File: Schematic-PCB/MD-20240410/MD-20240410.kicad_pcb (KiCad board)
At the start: 2 copper layers, 100.5 x 56.4 mm, 52 parts, among them J1 Conn_01x05_Pin, J2 Conn_01x04_Pin, J3 Conn_01x02_Pin, J4 Conn_01x02_Pin, J5 Conn_01x02_Pin, J6 Conn_01x02_Pin, J7 Conn_01x02_Pin, J8 Conn_01x15_Pin, Q2 PMOS, Q3 NMOS, Q4 NMOS

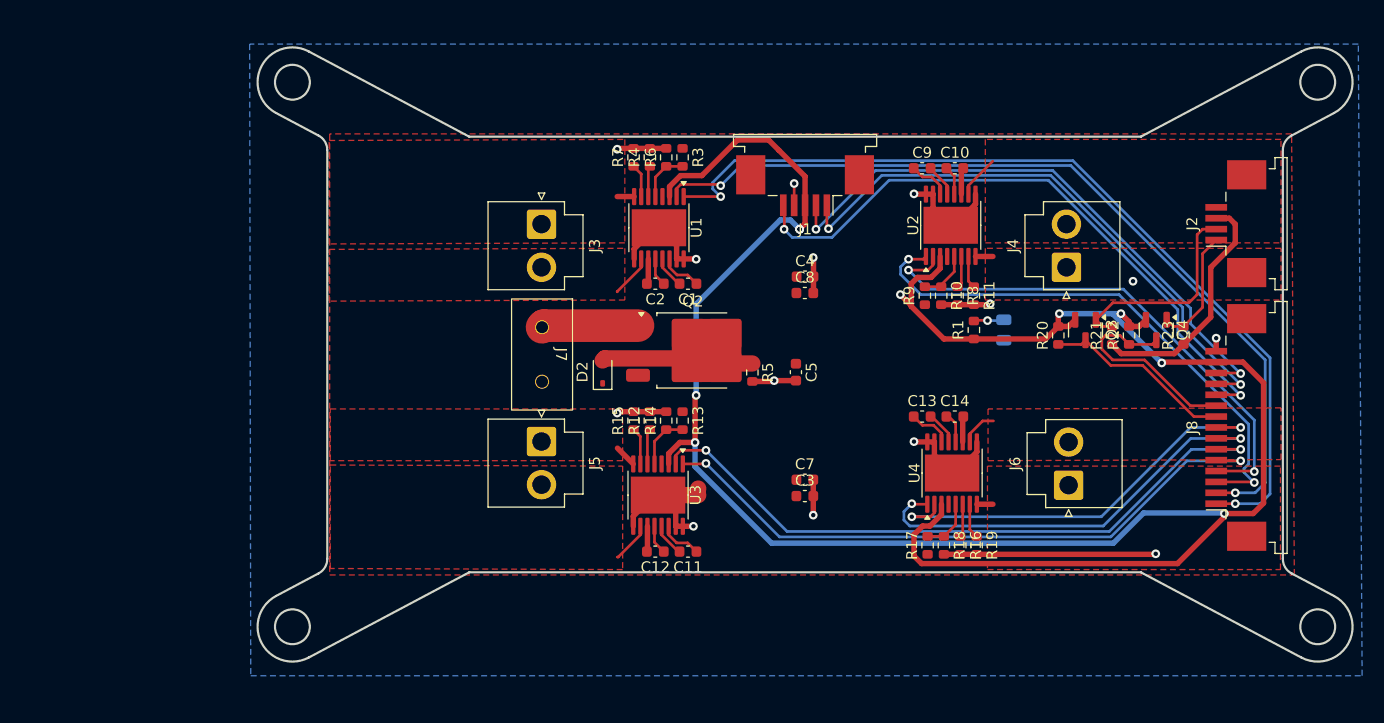
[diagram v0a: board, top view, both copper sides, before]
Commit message: MD回路のDR修正版-1
SLEEPは修正していません
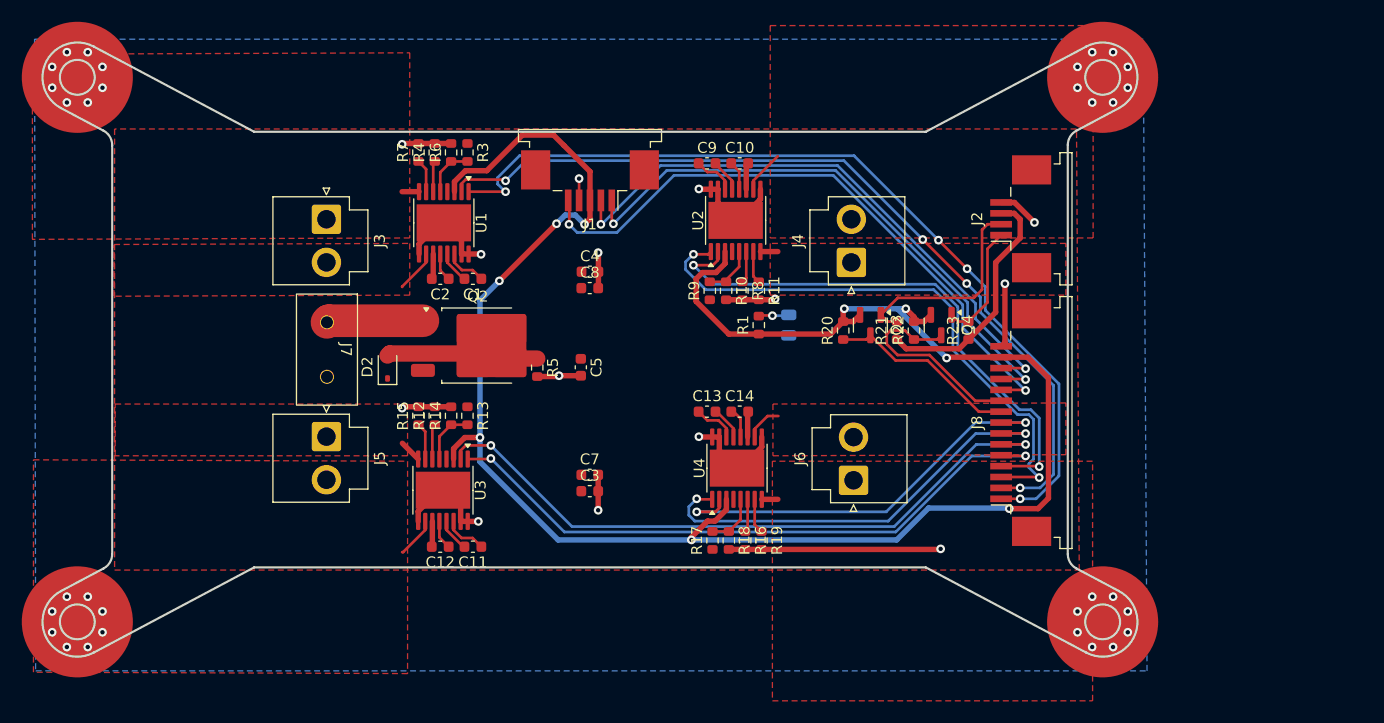
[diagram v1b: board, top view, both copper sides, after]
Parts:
- moved U1 19.8 mm to (116.8, 75.4)
- moved C1 19.8 mm to (119.5, 80.5)
- moved C10 19.8 mm to (144.0, 70.0)
- moved C11 19.8 mm to (119.5, 105.2)
- moved C12 19.8 mm to (116.5, 105.2)
- moved C13 19.8 mm to (141.0, 92.8)
- moved C14 19.8 mm to (144.0, 92.8)
- moved C2 19.8 mm to (116.5, 80.5)
- moved C3 19.8 mm to (130.2, 100.0)
- moved C4 19.8 mm to (130.2, 79.9)
- moved C5 19.8 mm to (129.4, 88.7)
- moved C7 19.8 mm to (130.2, 98.5)
- moved C8 19.8 mm to (130.2, 81.4)
- moved C9 19.8 mm to (141.0, 70.0)
- moved D1 19.8 mm to (148.5, 84.8)
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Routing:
- net +3.3V: track 209.8 -> 176.8 mm
- net GND: track 87.5 -> 92.4 mm, vias 14 -> 46
- net EN-2: track 50.5 -> 52.7 mm
- net PH-2: track 48.9 -> 51.0 mm
- net EN-1: track 82.3 -> 81.9 mm, vias 2 -> 4
- net PH-1: track 79.3 -> 78.9 mm, vias 2 -> 4

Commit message: Auto stash before merge of "main" and "origin/main"
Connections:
- J1 pad 3: +3.3V -> SLEEP-1
- J8 pad 14: +3.3V -> SLEEP-1
- Q3 pad 2: +3.3V -> SLEEP-1
- Q4 pad 2: +3.3V -> SLEEP-1
- R1 pad 1: +3.3V -> SLEEP-1
- R13 pad 1: SLEEP-3 -> SLEEP-1
- R17 pad 1: SLEEP-4 -> SLEEP-1
- R20 pad 2: +3.3V -> SLEEP-1
- R22 pad 2: +3.3V -> SLEEP-1
- R9 pad 1: SLEEP-2 -> SLEEP-1
- U1 pad 3: +3.3V -> SLEEP-1
- U2 pad 3: +3.3V -> SLEEP-1
- U3 pad 3: +3.3V -> SLEEP-1
- U4 pad 3: +3.3V -> SLEEP-1
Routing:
- net SLEEP-1: track 0.00 -> 187.9 mm, vias 0 -> 9
- net +3.3V: track 176.8 -> 0.00 mm, vias 9 -> 0

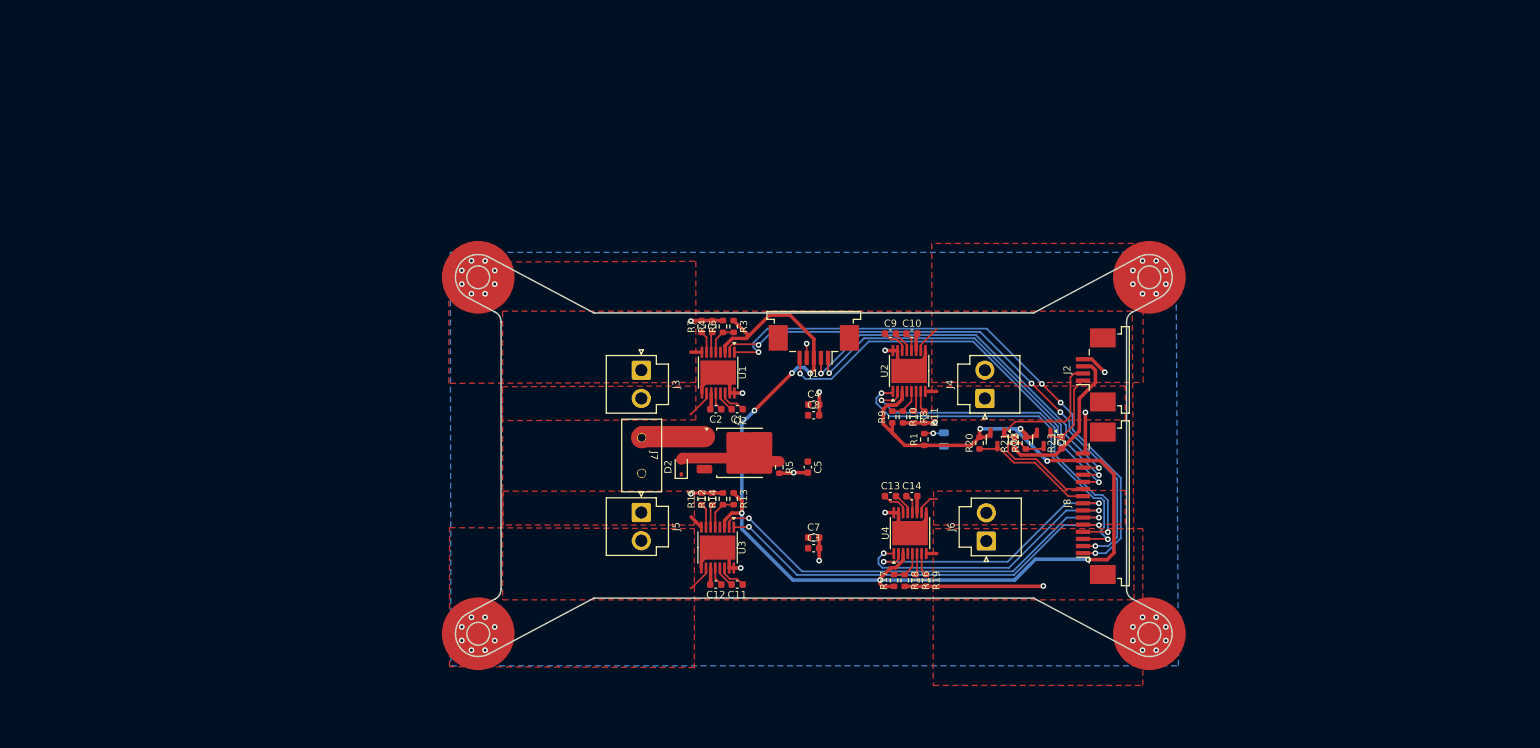
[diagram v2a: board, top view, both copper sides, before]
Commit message: MDの回路図/PCBを更新
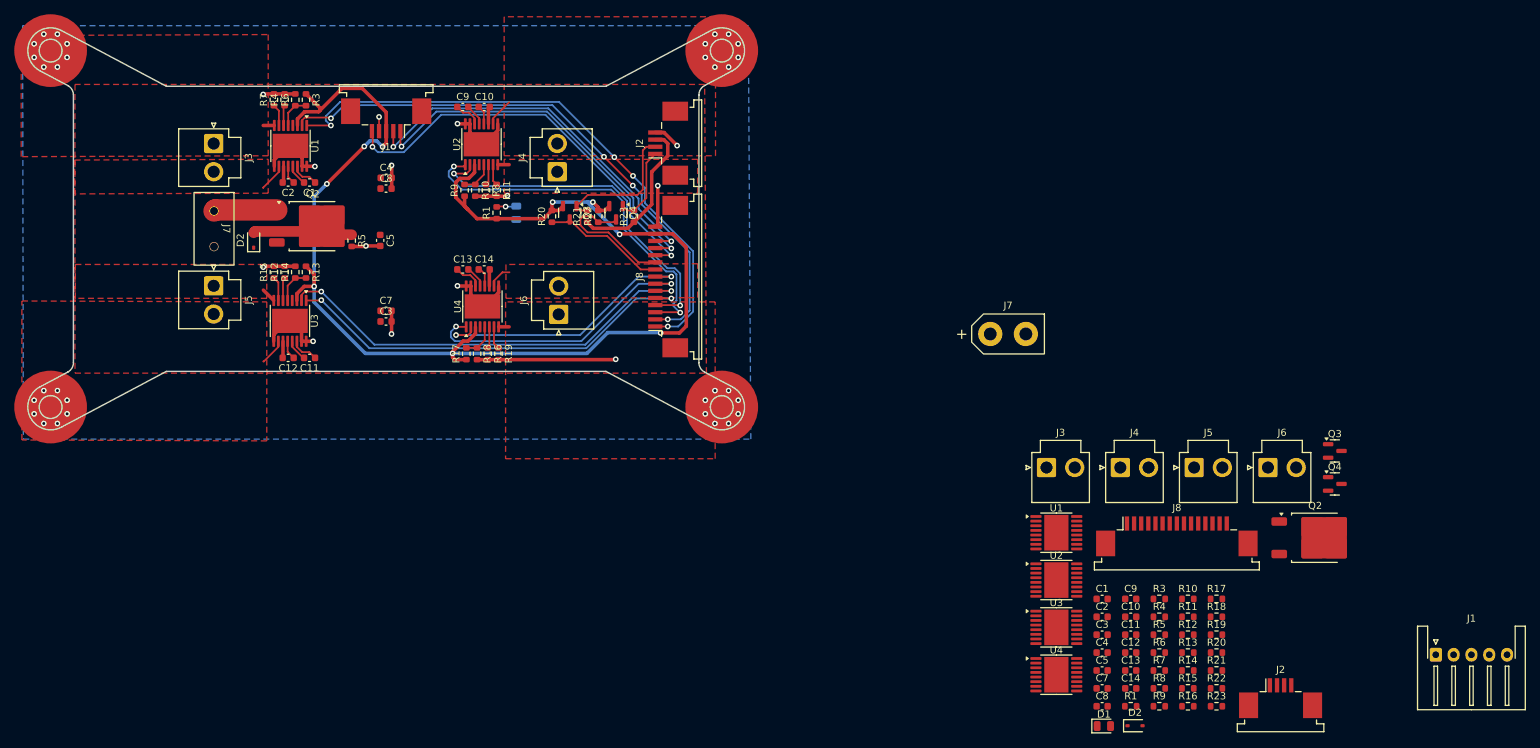
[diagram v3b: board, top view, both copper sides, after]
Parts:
- removed the C1 at (119.5, 80.5)
- removed the C10 at (144.0, 70.0)
- removed the C11 at (119.5, 105.2)
- removed the C12 at (116.5, 105.2)
- removed the C13 at (141.0, 92.8)
- removed the C14 at (144.0, 92.8)
- removed the C2 at (116.5, 80.5)
- removed the C3 at (130.2, 100.0)
- removed the C4 at (130.2, 79.9)
- removed the C5 at (129.4, 88.7)
- removed the C7 at (130.2, 98.5)
- removed the C8 at (130.2, 81.4)
- removed the C9 at (141.0, 70.0)
- removed the D1 at (148.5, 84.8)
- removed the D2 at (111.7, 88.7)
- removed the J1 at (130.2, 71.5)
- removed the J2 at (169.8, 75.0)
- removed the J3 at (106.0, 75.1)
- removed the J4 at (154.2, 79.0)
- removed the J5 at (106.0, 95.0)
- removed the J6 at (154.4, 99.0)
- removed the J7 at (106.1, 87.0)
- removed the J8 at (169.8, 93.8)
- removed the Q2 at (120.0, 86.7)
- removed the Q3 at (156.0, 84.8)
- removed the Q4 at (162.5, 84.8)
- removed the R1 at (145.8, 84.8)
- removed the R10 at (142.8, 81.7)
- removed the R11 at (145.8, 81.7)
- removed the R12 at (116.0, 93.1)
- removed the R13 at (119.0, 93.1)
- removed the R14 at (117.5, 93.1)
- removed the R15 at (114.5, 93.1)
- removed the R16 at (144.5, 104.6)
- removed the R17 at (141.5, 104.6)
- removed the R18 at (143.0, 104.6)
- removed the R19 at (146.0, 104.6)
- removed the R20 at (153.5, 85.3)
- removed the R21 at (158.4, 85.3)
- removed the R22 at (160.0, 85.3)
- removed the R23 at (165.0, 85.3)
- removed the R3 at (119.0, 69.0)
- removed the R4 at (116.0, 69.0)
- removed the R5 at (125.4, 88.7)
- removed the R6 at (117.5, 69.0)
- removed the R7 at (114.5, 69.0)
- removed the R8 at (144.2, 81.7)
- removed the R9 at (141.2, 81.7)
- removed the U1 at (116.8, 75.4)
- removed the U2 at (143.6, 75.2)
- removed the U3 at (116.8, 100.0)
- removed the U4 at (143.8, 97.9)
- added C1: 22n, Capacitor_SMD:C_0603_1608Metric, F.Cu at (59.5, 48.8)
- added C1: 22n, Capacitor_SMD:C_0603_1608Metric, F.Cu at (170.7, 107.2)
- added C10: 220n, Capacitor_SMD:C_0603_1608Metric, F.Cu at (174.7, 109.7)
- added C10: 220n, Capacitor_SMD:C_0603_1608Metric, F.Cu at (84.0, 38.1)
- added C11: 22n, Capacitor_SMD:C_0603_1608Metric, F.Cu at (174.7, 112.2)
- added C11: 22n, Capacitor_SMD:C_0603_1608Metric, F.Cu at (59.5, 73.3)
- added C12: 220n, Capacitor_SMD:C_0603_1608Metric, F.Cu at (174.7, 114.7)
- added C12: 220n, Capacitor_SMD:C_0603_1608Metric, F.Cu at (56.5, 73.3)
- added C13: 22n, Capacitor_SMD:C_0603_1608Metric, F.Cu at (174.7, 117.2)
- added C13: 22n, Capacitor_SMD:C_0603_1608Metric, F.Cu at (81.0, 61.0)
- added C14: 220n, Capacitor_SMD:C_0603_1608Metric, F.Cu at (174.7, 119.7)
- added C14: 220n, Capacitor_SMD:C_0603_1608Metric, F.Cu at (84.0, 61.0)
- added C2: 220n, Capacitor_SMD:C_0603_1608Metric, F.Cu at (56.5, 48.8)
- added C2: 220n, Capacitor_SMD:C_0603_1608Metric, F.Cu at (170.7, 109.7)
- added C3: 4.7u, Capacitor_SMD:C_0603_1608Metric, F.Cu at (70.2, 68.2)
- added C3: 4.7u, Capacitor_SMD:C_0603_1608Metric, F.Cu at (170.7, 112.2)
- added C4: 4.7u, Capacitor_SMD:C_0603_1608Metric, F.Cu at (70.3, 48.1)
- added C4: 4.7u, Capacitor_SMD:C_0603_1608Metric, F.Cu at (170.7, 114.7)
- added C5: 50u, Capacitor_SMD:C_0603_1608Metric, F.Cu at (69.4, 56.9)
- added C5: 50u, Capacitor_SMD:C_0603_1608Metric, F.Cu at (170.7, 117.2)
- added C7: 0.1u, Capacitor_SMD:C_0603_1608Metric, F.Cu at (70.2, 66.8)
- added C7: 0.1u, Capacitor_SMD:C_0603_1608Metric, F.Cu at (170.7, 119.7)
- added C8: 0.1u, Capacitor_SMD:C_0603_1608Metric, F.Cu at (70.2, 49.6)
- added C8: 0.1u, Capacitor_SMD:C_0603_1608Metric, F.Cu at (170.7, 122.2)
- added C9: 22n, Capacitor_SMD:C_0603_1608Metric, F.Cu at (174.7, 107.2)
- added C9: 22n, Capacitor_SMD:C_0603_1608Metric, F.Cu at (81.0, 38.1)
- added D1: LED, LED_SMD:LED_0805_2012Metric, F.Cu at (170.9, 125.0)
- added D1: LED, LED_SMD:LED_0805_2012Metric, B.Cu at (88.5, 53.0)
- added D2: 16.2V, Diode_SMD:D_SOD-323, F.Cu at (175.3, 125.0)
- added D2: 16.2V, Diode_SMD:D_SOD-323, F.Cu at (51.7, 56.9)
- added J1: Conn_01x05_Pin, Connector_JST:JST_XH_S5B-XH-A-1_1x05_P2.50mm_Horizontal, F.Cu at (217.5, 115.0)
- added J1: Conn_01x05_Pin, Connector_FFC-FPC:TE_84953-5_1x05-1MP_P1.0mm_Horizontal, F.Cu at (70.3, 39.8)
- added J2: Conn_01x04_Pin, Connector_FFC-FPC:TE_84953-4_1x04-1MP_P1.0mm_Horizontal, F.Cu at (195.7, 121.1)
- added J2: Conn_01x04_Pin, Connector_FFC-FPC:TE_84953-4_1x04-1MP_P1.0mm_Horizontal, F.Cu at (109.8, 43.2)
- added J3: Conn_01x02_Pin, Connector_JST:JST_VH_B2P-VH_1x02_P3.96mm_Vertical, F.Cu at (162.9, 88.7)
- added J3: Conn_01x02_Pin, Connector_JST:JST_VH_B2P-VH_1x02_P3.96mm_Vertical, F.Cu at (46.1, 43.3)
- added J4: Conn_01x02_Pin, Connector_JST:JST_VH_B2P-VH_1x02_P3.96mm_Vertical, F.Cu at (173.2, 88.7)
- added J4: Conn_01x02_Pin, Connector_JST:JST_VH_B2P-VH_1x02_P3.96mm_Vertical, F.Cu at (94.3, 47.2)
- added J5: Conn_01x02_Pin, Connector_JST:JST_VH_B2P-VH_1x02_P3.96mm_Vertical, F.Cu at (183.6, 88.7)
- added J5: Conn_01x02_Pin, Connector_JST:JST_VH_B2P-VH_1x02_P3.96mm_Vertical, F.Cu at (46.1, 63.2)
- added J6: Conn_01x02_Pin, Connector_JST:JST_VH_B2P-VH_1x02_P3.96mm_Vertical, F.Cu at (194.0, 88.7)
- added J6: Conn_01x02_Pin, Connector_JST:JST_VH_B2P-VH_1x02_P3.96mm_Vertical, F.Cu at (94.5, 67.2)
- added J7: Conn_01x02_Pin, @MyLibrary:XT30U-M, F.Cu at (46.1, 55.2)
- added J7: Conn_01x02_Pin, @2024-MD:XT30U-M, F.Cu at (157.5, 70.0)
- added J8: Conn_01x15_Pin, Connector_FFC-FPC:TE_1-84953-5_1x15-1MP_P1.0mm_Horizontal, F.Cu at (181.2, 98.4)
- added J8: Conn_01x15_Pin, Connector_FFC-FPC:TE_1-84953-5_1x15-1MP_P1.0mm_Horizontal, F.Cu at (109.8, 62.0)
- added Q2: PMOS, Package_TO_SOT_SMD:TO-252-2, F.Cu at (200.6, 98.6)
- added Q2: PMOS, Package_TO_SOT_SMD:TO-252-2, F.Cu at (60.0, 54.9)
- added Q3: NMOS, Package_TO_SOT_SMD:SOT-23, F.Cu at (203.3, 86.4)
- added Q3: NMOS, Package_TO_SOT_SMD:SOT-23, F.Cu at (96.0, 53.0)
- added Q4: NMOS, Package_TO_SOT_SMD:SOT-23, F.Cu at (102.5, 53.0)
- added Q4: NMOS, Package_TO_SOT_SMD:SOT-23, F.Cu at (203.3, 91.0)
- added R1: 330, Resistor_SMD:R_0603_1608Metric, F.Cu at (174.7, 122.2)
- added R1: 330, Resistor_SMD:R_0603_1608Metric, F.Cu at (85.8, 53.0)
- added R10: NP, Resistor_SMD:R_0603_1608Metric, F.Cu at (182.7, 107.2)
- added R10: NP, Resistor_SMD:R_0603_1608Metric, F.Cu at (82.8, 49.9)
- added R11: 20k, Resistor_SMD:R_0603_1608Metric, F.Cu at (182.7, 109.7)
- added R11: 20k, Resistor_SMD:R_0603_1608Metric, F.Cu at (85.8, 49.9)
- added R12: 2.49k, Resistor_SMD:R_0603_1608Metric, F.Cu at (182.7, 112.2)
- added R12: 2.49k, Resistor_SMD:R_0603_1608Metric, F.Cu at (56.0, 61.3)
- added R13: 10k, Resistor_SMD:R_0603_1608Metric, F.Cu at (182.7, 114.7)
- added R13: 10k, Resistor_SMD:R_0603_1608Metric, F.Cu at (59.0, 61.3)
- added R14: NP, Resistor_SMD:R_0603_1608Metric, F.Cu at (57.5, 61.3)
- added R14: NP, Resistor_SMD:R_0603_1608Metric, F.Cu at (182.7, 117.2)
- added R15: 20k, Resistor_SMD:R_0603_1608Metric, F.Cu at (54.5, 61.3)
- added R15: 20k, Resistor_SMD:R_0603_1608Metric, F.Cu at (182.7, 119.7)
- added R16: 2.49k, Resistor_SMD:R_0603_1608Metric, F.Cu at (182.7, 122.2)
- added R16: 2.49k, Resistor_SMD:R_0603_1608Metric, F.Cu at (84.5, 72.8)
- added R17: 10k, Resistor_SMD:R_0603_1608Metric, F.Cu at (81.5, 72.8)
- added R17: 10k, Resistor_SMD:R_0603_1608Metric, F.Cu at (186.7, 107.2)
- added R18: NP, Resistor_SMD:R_0603_1608Metric, F.Cu at (83.0, 72.8)
- added R18: NP, Resistor_SMD:R_0603_1608Metric, F.Cu at (186.7, 109.7)
- added R19: 20k, Resistor_SMD:R_0603_1608Metric, F.Cu at (86.0, 72.8)
- added R19: 20k, Resistor_SMD:R_0603_1608Metric, F.Cu at (186.7, 112.2)
- added R20: 10k, Resistor_SMD:R_0603_1608Metric, F.Cu at (186.7, 114.7)
- added R20: 10k, Resistor_SMD:R_0603_1608Metric, F.Cu at (93.5, 53.5)
- added R21: 10k, Resistor_SMD:R_0603_1608Metric, F.Cu at (186.7, 117.2)
- added R21: 10k, Resistor_SMD:R_0603_1608Metric, F.Cu at (98.4, 53.5)
- added R22: 10k, Resistor_SMD:R_0603_1608Metric, F.Cu at (186.7, 119.7)
- added R22: 10k, Resistor_SMD:R_0603_1608Metric, F.Cu at (100.0, 53.5)
- added R23: 10k, Resistor_SMD:R_0603_1608Metric, F.Cu at (186.7, 122.2)
- added R23: 10k, Resistor_SMD:R_0603_1608Metric, F.Cu at (105.0, 53.5)
- added R3: 10k, Resistor_SMD:R_0603_1608Metric, F.Cu at (59.0, 37.1)
- added R3: 10k, Resistor_SMD:R_0603_1608Metric, F.Cu at (178.7, 107.2)
- added R4: 2.49k, Resistor_SMD:R_0603_1608Metric, F.Cu at (178.7, 109.7)
- added R4: 2.49k, Resistor_SMD:R_0603_1608Metric, F.Cu at (56.0, 37.1)
- added R5: 100k, Resistor_SMD:R_0603_1608Metric, F.Cu at (65.4, 56.9)
- added R5: 100k, Resistor_SMD:R_0603_1608Metric, F.Cu at (178.7, 112.2)
- added R6: NP, Resistor_SMD:R_0603_1608Metric, F.Cu at (57.5, 37.1)
- added R6: NP, Resistor_SMD:R_0603_1608Metric, F.Cu at (178.7, 114.7)
- added R7: 20k, Resistor_SMD:R_0603_1608Metric, F.Cu at (54.5, 37.1)
- added R7: 20k, Resistor_SMD:R_0603_1608Metric, F.Cu at (178.7, 117.2)
- added R8: 2.49k, Resistor_SMD:R_0603_1608Metric, F.Cu at (178.7, 119.7)
- added R8: 2.49k, Resistor_SMD:R_0603_1608Metric, F.Cu at (84.3, 49.9)
- added R9: 10k, Resistor_SMD:R_0603_1608Metric, F.Cu at (81.3, 49.9)
- added R9: 10k, Resistor_SMD:R_0603_1608Metric, F.Cu at (178.7, 122.2)
- added U1: ~, Package_SO:HTSSOP-16-1EP_4.4x5mm_P0.65mm_EP3.4x5mm_Mask2.46x2.31mm, F.Cu at (164.3, 97.9)
- added U1: ~, Package_SO:HTSSOP-16-1EP_4.4x5mm_P0.65mm_EP3.4x5mm_Mask2.46x2.31mm, F.Cu at (56.8, 43.6)
- added U2: ~, Package_SO:HTSSOP-16-1EP_4.4x5mm_P0.65mm_EP3.4x5mm_Mask2.46x2.31mm, F.Cu at (164.3, 104.5)
- added U2: ~, Package_SO:HTSSOP-16-1EP_4.4x5mm_P0.65mm_EP3.4x5mm_Mask2.46x2.31mm, F.Cu at (83.6, 43.4)
- added U3: ~, Package_SO:HTSSOP-16-1EP_4.4x5mm_P0.65mm_EP3.4x5mm_Mask2.46x2.31mm, F.Cu at (164.3, 111.2)
- added U3: ~, Package_SO:HTSSOP-16-1EP_4.4x5mm_P0.65mm_EP3.4x5mm_Mask2.46x2.31mm, F.Cu at (56.8, 68.2)
- added U4: ~, Package_SO:HTSSOP-16-1EP_4.4x5mm_P0.65mm_EP3.4x5mm_Mask2.46x2.31mm, F.Cu at (83.8, 66.1)
- added U4: ~, Package_SO:HTSSOP-16-1EP_4.4x5mm_P0.65mm_EP3.4x5mm_Mask2.46x2.31mm, F.Cu at (164.3, 117.8)

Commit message: MD基板のPCBを更新
回路図のDRを再度お願いしたい
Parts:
- removed the C1 at (59.5, 48.8)
- removed the C10 at (84.0, 38.1)
- removed the C11 at (59.5, 73.3)
- removed the C12 at (56.5, 73.3)
- removed the C13 at (81.0, 61.0)
- removed the C14 at (84.0, 61.0)
- removed the C2 at (56.5, 48.8)
- removed the C3 at (70.2, 68.2)
- removed the C3 at (170.7, 112.2)
- removed the C4 at (70.3, 48.1)
- removed the C4 at (170.7, 114.7)
- removed the C5 at (69.4, 56.9)
- removed the C5 at (170.7, 117.2)
- removed the C7 at (70.2, 66.8)
- removed the C7 at (170.7, 119.7)
- removed the C8 at (70.2, 49.6)
- removed the C8 at (170.7, 122.2)
- removed the C9 at (81.0, 38.1)
- removed the D1 at (170.9, 125.0)
- removed the D1 at (88.5, 53.0)
- removed D2 (x2): 16.2V, Diode_SMD:D_SOD-323
- removed J1: Conn_01x05_Pin, Connector_FFC-FPC:TE_84953-5_1x05-1MP_P1.0mm_Horizontal
- removed J2 (x2): Conn_01x04_Pin, Connector_FFC-FPC:TE_84953-4_1x04-1MP_P1.0mm_Horizontal
- removed the J3 at (162.9, 88.7)
- removed the J3 at (46.1, 43.3)
- removed the J4 at (94.3, 47.2)
- removed the J5 at (46.1, 63.2)
- removed the J6 at (94.5, 67.2)
- removed J7: Conn_01x02_Pin, @MyLibrary:XT30U-M
- removed J7: Conn_01x02_Pin, @2024-MD:XT30U-M
- removed the J8 at (181.2, 98.4)
- removed the J8 at (109.8, 62.0)
- removed Q2 (x2): PMOS, Package_TO_SOT_SMD:TO-252-2
- removed the Q3 at (96.0, 53.0)
- removed the Q4 at (102.5, 53.0)
- removed the R1 at (174.7, 122.2)
- removed the R1 at (85.8, 53.0)
- removed the R10 at (82.8, 49.9)
- removed the R11 at (85.8, 49.9)
- removed the R12 at (56.0, 61.3)
- removed the R13 at (59.0, 61.3)
- removed the R14 at (57.5, 61.3)
- removed the R15 at (54.5, 61.3)
- removed the R16 at (84.5, 72.8)
- removed the R17 at (81.5, 72.8)
- removed the R18 at (83.0, 72.8)
- removed the R19 at (86.0, 72.8)
- removed the R20 at (186.7, 114.7)
- removed the R20 at (93.5, 53.5)
- removed the R21 at (186.7, 117.2)
- removed the R21 at (98.4, 53.5)
- removed the R22 at (186.7, 119.7)
- removed the R22 at (100.0, 53.5)
- removed the R23 at (186.7, 122.2)
- removed the R23 at (105.0, 53.5)
- removed the R3 at (59.0, 37.1)
- removed the R4 at (56.0, 37.1)
- removed R5 (x2): 100k, Resistor_SMD:R_0603_1608Metric
- removed the R6 at (57.5, 37.1)
- removed the R7 at (54.5, 37.1)
- removed the R8 at (84.3, 49.9)
- removed the R9 at (81.3, 49.9)
- removed the U1 at (56.8, 43.6)
- removed the U2 at (83.6, 43.4)
- removed the U3 at (56.8, 68.2)
- removed the U4 at (83.8, 66.1)
- added C3: 4.7u, Capacitor_SMD:C_0603_1608Metric, F.Cu at (99.5, -3.35)
- added C4: 4.7u, Capacitor_SMD:C_0603_1608Metric, F.Cu at (99.5, -0.84)
- added C5: 50u, Capacitor_SMD:C_0603_1608Metric, F.Cu at (99.5, 1.67)
- added C7: 0.1u, Capacitor_SMD:C_0603_1608Metric, F.Cu at (99.5, 4.18)
- added C8: 0.1u, Capacitor_SMD:C_0603_1608Metric, F.Cu at (99.5, 6.69)
- added D1: LED, LED_SMD:LED_0805_2012Metric, B.Cu at (3.50, 3.00)
- added J3: Conn_01x02_Pin, @2024-MD:JST_VH_B2P-VH-B_1x02_P3.96mm_Vertical, F.Cu at (-37.6, -15.6)
- added J8: Conn_01x15_Pin, Connector_FFC-FPC:TE_1-84953-5_1x15-1MP_P1.0mm_Horizontal, F.Cu at (0.00, 0.00)
- added LINE: Conn_01x04_Pin, Connector_JST:JST_XH_S4B-XH-A-1_1x04_P2.50mm_Horizontal, F.Cu at (36.1, 3.75)
- added R1: 330, Resistor_SMD:R_0603_1608Metric, F.Cu at (103.5, -3.35)
- added R20: 10k, Resistor_SMD:R_0603_1608Metric, F.Cu at (28.5, -4.50)
- added R21: 10k, Resistor_SMD:R_0603_1608Metric, F.Cu at (28.5, -6.00)
- added R22: 10k, Resistor_SMD:R_0603_1608Metric, F.Cu at (29.0, 4.50)
- added R23: 10k, Resistor_SMD:R_0603_1608Metric, F.Cu at (29.0, 6.00)
- added VIN: Conn_01x02_Pin, @2024-MD:XT30U-M, F.Cu at (0.00, 16.0)
- J4, J5, J6: footprint Connector_JST:JST_VH_B2P-VH_1x02_P3.96mm_Vertical -> @2024-MD:JST_VH_B2P-VH-B_1x02_P3.96mm_Vertical
- moved KICKER 250.2 mm to (5.00, -17.1), turned to 180 degrees
- moved R7 245.0 mm to (-25.8, -17.8), turned to 90 degrees
- moved R6 241.1 mm to (-22.8, -17.8), turned to 90 degrees
- moved R4 239.7 mm to (-24.2, -17.8), turned to 90 degrees
- moved R3 235.8 mm to (-21.2, -17.8), turned to 90 degrees
- moved R11 232.7 mm to (-25.8, 6.25), turned to 90 degrees
- moved R8 232.5 mm to (-24.2, 6.25), turned to 90 degrees
- moved R9 231.2 mm to (-21.2, 6.25), turned to 90 degrees
- moved R10 228.9 mm to (-22.8, 6.25), turned to -90 degrees
- moved C2 228.1 mm to (-25.2, -7.25), turned to 180 degrees
- moved C1 224.3 mm to (-22.2, -7.25), turned to 180 degrees
- moved J4 223.2 mm to (-37.6, 15.6), turned to 135 degrees
- moved C10 220.4 mm to (-25.2, 16.8), turned to 180 degrees
- moved U1 218.9 mm to (-25.0, -12.0), turned to -90 degrees
- moved C9 216.7 mm to (-22.2, 16.8), turned to 180 degrees
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- renumbered J1 to KICKER
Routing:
- net SLEEP-1: track 187.9 -> 15.8 mm, vias 9 -> 4
- net GND: track 92.4 -> 0.00 mm, vias 46 -> 0
- net EN-1: track 81.9 -> 0.00 mm, vias 4 -> 0
- net PH-1: track 78.9 -> 0.00 mm, vias 4 -> 0
- net PH-3: track 61.3 -> 0.00 mm, vias 2 -> 0
- net EN-3: track 59.2 -> 0.00 mm, vias 2 -> 0
- net EN-2: track 52.7 -> 0.00 mm, vias 2 -> 0
- net PH-2: track 51.0 -> 0.00 mm, vias 2 -> 0
- net ball01k: track 58.4 -> 17.8 mm, vias 2 -> 0
- net EN-4: track 40.0 -> 0.00 mm, vias 2 -> 0
- net PH-4: track 38.9 -> 0.00 mm, vias 2 -> 0
- net KickerSignal-main: track 54.3 -> 15.6 mm, vias 2 -> 0
- net ball02k: track 53.4 -> 16.2 mm, vias 2 -> 0
- net Net-(D2-A): track 14.6 -> 0.00 mm
- net Line-MD-Main=RX_3.3V: track 17.6 -> 30.0 mm, vias 0 -> 2
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- removed copper zone on F.Cu, net OUT1-1
- removed copper zone on F.Cu, net OUT1-2
- removed copper zone on F.Cu, net OUT1-3
- removed copper zone on F.Cu, net OUT1-4
- removed copper zone on F.Cu, net OUT2-1
- removed copper zone on F.Cu, net OUT2-2
- removed copper zone on F.Cu, net OUT2-3
- removed copper zone on F.Cu, net OUT2-4
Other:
- outline, holes or cut-outs redrawn
